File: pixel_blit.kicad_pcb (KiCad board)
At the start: 4 copper layers, 175.5 x 122 mm, 193 parts, among them CN1 PJ-3059-B, CN2 PJ-3059-B, J1 Conn_01x03_Pin, SW1 K2-1808SN-A4SW, SW2 DSWB04LHGET, SW3 K2-1808SN-A4SW, SW4 K2-1808SN-A4SW, U1 RP2350B_C42415655, U10 DB301V-3.5-3P-GN, U11 DB301V-3.5-3P-GN, U12 DB301V-3.5-3P-GN, U13 DB301V-3.5-3P-GN, U14 DB301V-3.5-3P-GN, U15 DB301V-3.5-3P-GN, U16 DB301V-3.5-3P-GN, U17 DB301V-3.5-3P-GN, U18 DB301V-3.5-3P-GN, U19 DB301V-3.5-3P-GN, U2 W25Q128JVSIQTR, U20 DB301V-3.5-3P-GN, U21 DB301V-3.5-3P-GN, U22 DB301V-3.5-3P-GN, U23 DB301V-3.5-3P-GN, U24 DB301V-3.5-3P-GN, U25 DB301V-3.5-3P-GN, U26 DB301V-3.5-3P-GN, U27 DB301V-3.5-3P-GN, U28 DB301V-3.5-3P-GN, U29 DB301V-3.5-3P-GN, U3 TPS63070RNMR, U30 DB301V-3.5-3P-GN, U31 DB301V-3.5-3P-GN, U32 DB301V-3.5-3P-GN, U33 DB301V-3.5-3P-GN, U34 DB301V-3.5-3P-GN, U35 DB301V-3.5-3P-GN, U36 DB301V-3.5-3P-GN, U37 DB301V-3.5-3P-GN, U38 DB301V-3.5-3P-GN, U39 DB301V-3.5-3P-GN, U40 DB301V-3.5-3P-GN, U41 DSLVDS1048PWR, U42 DSLVDS1047PWR, U43 DBT10-7.62-2P, U44 DBT10-7.62-2P, U45 DBT10-7.62-2P, U46 DBT10-7.62-2P, U47 2.54-1*4, U48 2.54-1*4, U49 2.54-1*4, U5 SN74LVC8T245PWR, U50 LMV358IDR, U6 SN74LVC8T245PWR, U7 SN74LVC8T245PWR, U8 SN74LVC8T245PWR, U9 DB301V-3.5-3P-GN

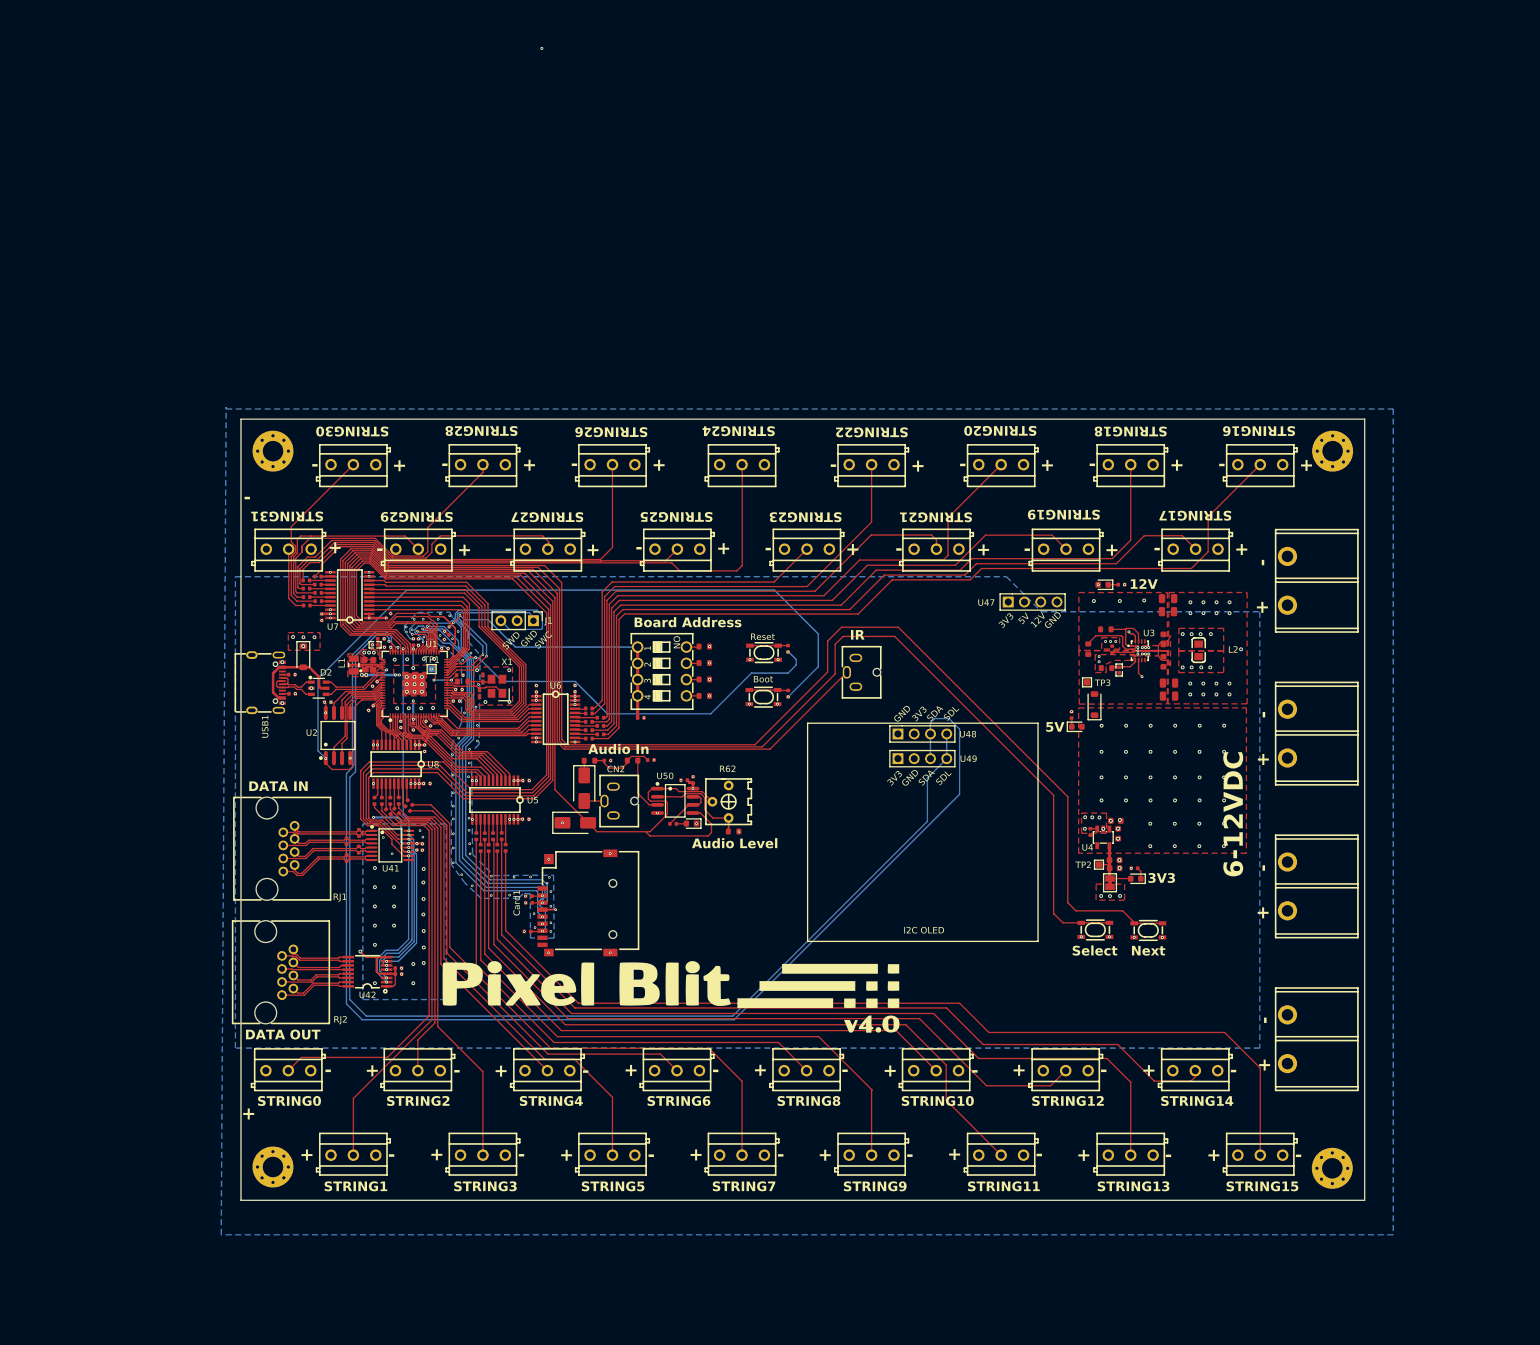
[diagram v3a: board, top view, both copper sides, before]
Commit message: Beef up power plane
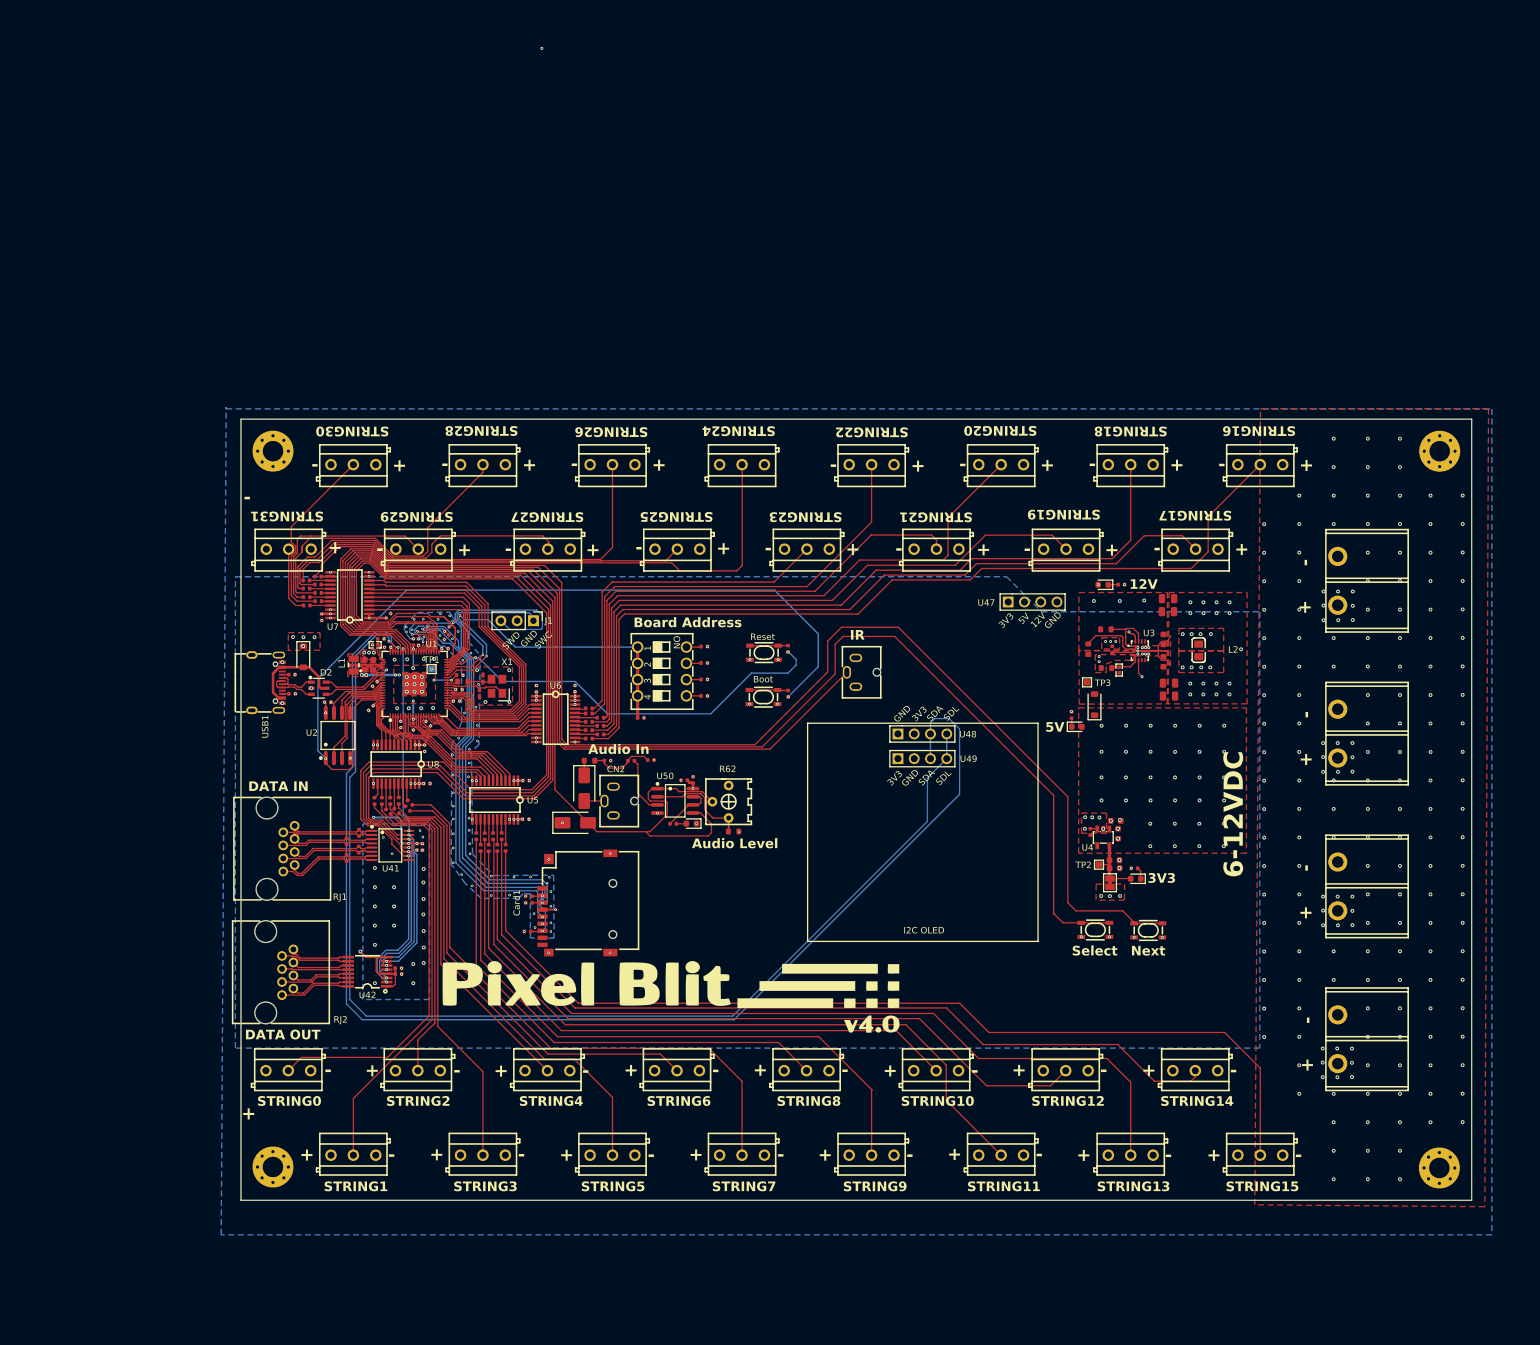
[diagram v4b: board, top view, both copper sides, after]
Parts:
- R2, R3, R4, R5, R66: footprint PCM_JLCPCB:R_0603 -> PCM_JLCPCB:R_0402
- moved H2 16.7 mm to (240.1, 36.2)
- moved H1 16.7 mm to (240.0, 148.2)
- moved U43 7.85 mm to (224.2, 56.4)
- moved U44 7.85 mm to (224.2, 80.3)
- moved U45 7.85 mm to (224.2, 104.2)
- moved U46 7.85 mm to (224.2, 128.0)
- moved R66 0.22 mm to (113.8, 84.5)
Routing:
- net +12V: vias 4 -> 192
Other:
- board size 175.5 x 122 mm -> 192.2 x 122 mm

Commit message: Library shuffle and Fabrication Toolkit micro adjustments
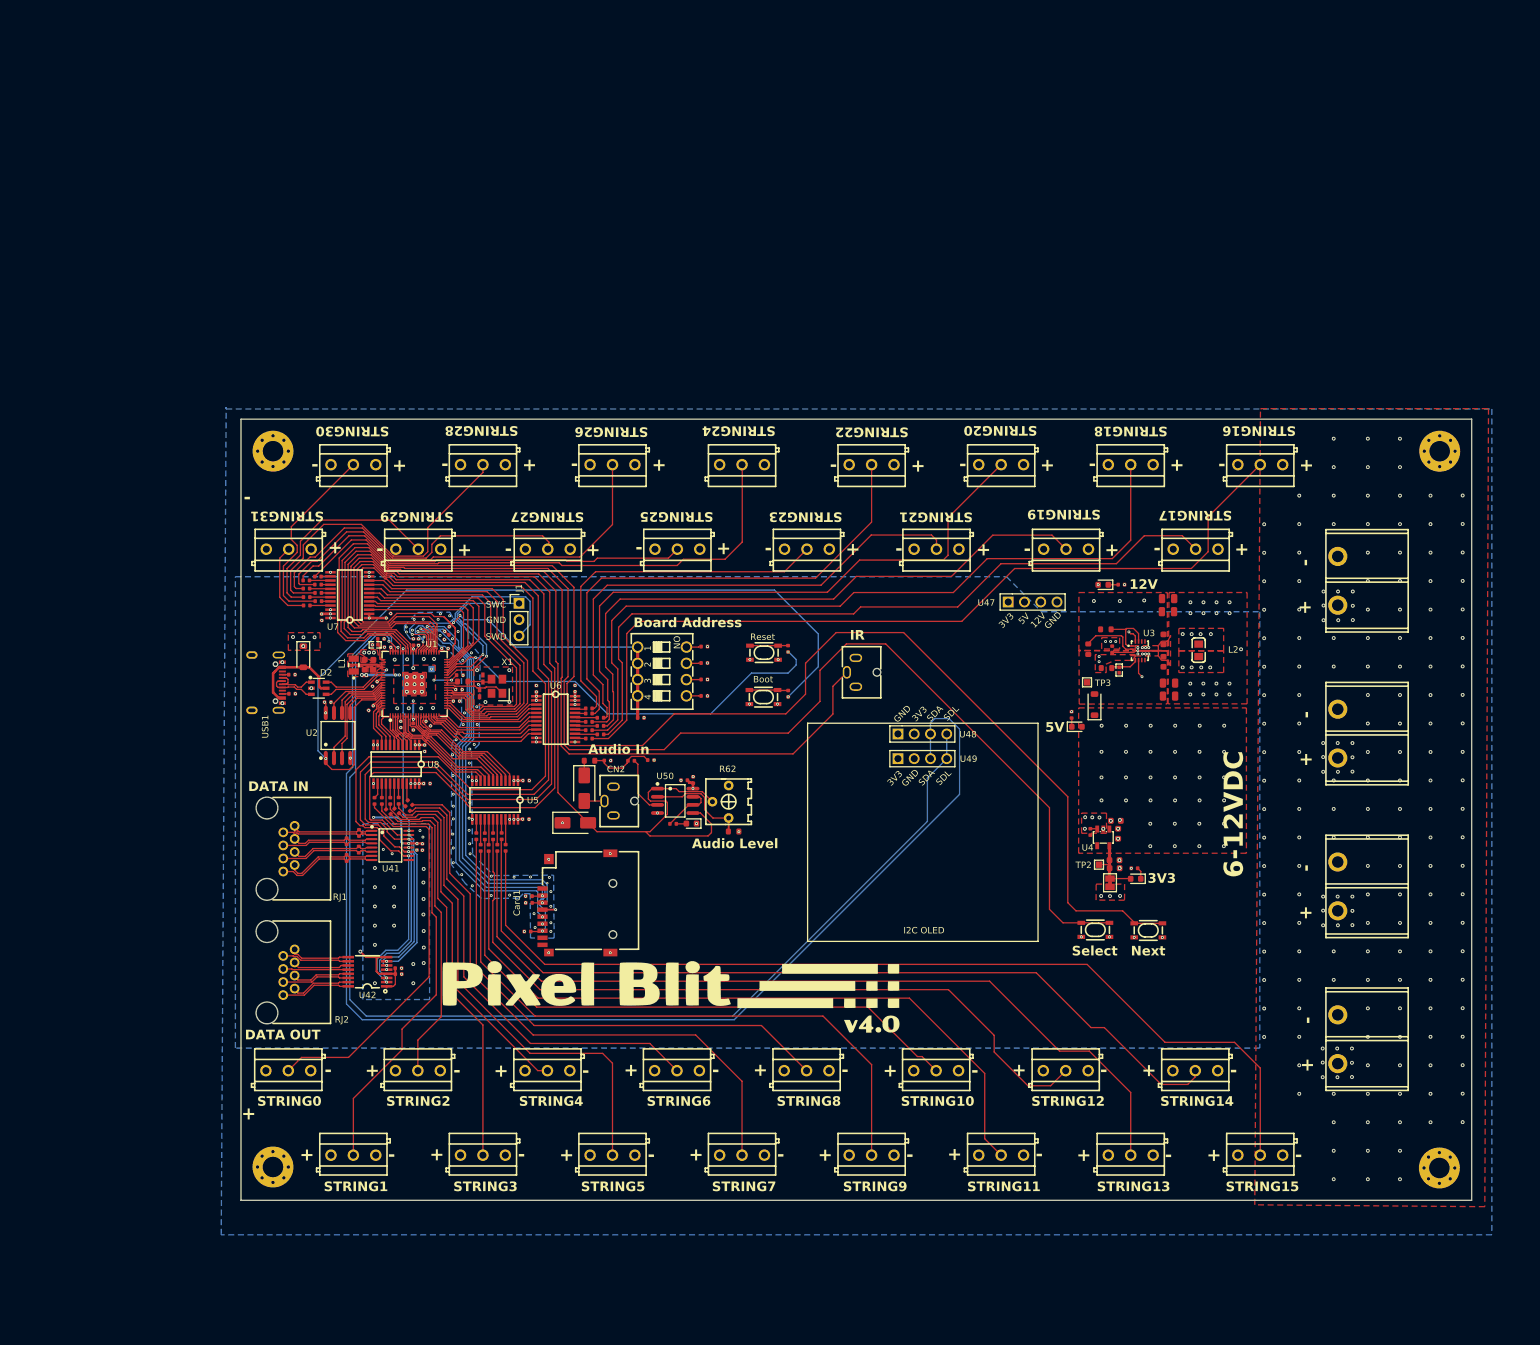
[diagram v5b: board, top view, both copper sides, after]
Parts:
- C1, C10, C11, C12, C13, C14, C2, C25, C3, C30, C31, C32, C33, C34, C35, C36, C37, C38, C39, C4, C40, C41, C42, C43, C44, C45, C5, C6, C7, C8, C9: footprint PCM_JLCPCB:C_0402 -> PixelBlit:C_0402
- C15, C16, C19, C24, C26, C27, C28, C29: footprint PCM_JLCPCB:C_0603 -> PixelBlit:C_0603
- C17, C18: footprint EasyEDA:C0402 -> PixelBlit:C0402
- C20, C21, C22, C23: footprint PCM_JLCPCB:C_0805 -> PixelBlit:C_0805
- CN1, CN2: footprint EasyEDA:AUDIO-TH_XKB_PJ-3059-B -> PixelBlit:AUDIO-TH_XKB_PJ-3059-B
- Card1: footprint EasyEDA:TF-SMD_TF-PUSH -> PixelBlit:TF-SMD_TF-PUSH
- D1, D3: footprint PCM_JLCPCB:D_SOD-123 -> PixelBlit:D_SOD-123
- D2: footprint EasyEDA:SOT-23-6_L2.9-W1.6-P0.95-LS2.8-BL -> PixelBlit:SOT-23-6_L2.9-W1.6-P0.95-LS2.8-BL
- D4, D5: footprint PCM_JLCPCB:D_SMA -> PixelBlit:D_SMA
- D6, PWR_LED1, PWR_LED2, PWR_LED3: footprint PCM_JLCPCB:D_0603 -> PixelBlit:D_0603
- G***: footprint EasyEDA:pixelblitlogo -> PixelBlit:pixelblitlogo
- H1, H2, H3, H4: footprint MountingHole:MountingHole_3.2mm_M3_Pad_Via -> PixelBlit:MountingHole_3.2mm_M3_Pad_Via
- J1: footprint Connector_PinHeader_2.54mm:PinHeader_1x03_P2.54mm_Vertical -> PixelBlit:PinHeader_1x03_P2.54mm_Vertical
- JP1: footprint Jumper:SolderJumper-2_P1.3mm_Bridged_Pad1.0x1.5mm -> PixelBlit:SolderJumper-2_P1.3mm_Bridged_Pad1.0x1.5mm
- L1: footprint EasyEDA:IND-SMD_L2.0-W1.6_AOTA-B201610S3R3-101-T -> PixelBlit:IND-SMD_L2.0-W1.6_AOTA-B201610S3R3-101-T
- L2: footprint EasyEDA:L0805 -> PixelBlit:L0805
- R1, R14, R15, R16, R17, R18, R19, R2, R20, R21, R22, R23, R24, R25, R26, R27, R28, R29, R3, R30, R31, R32, R33, R34, R35, R36, R37, R38, R39, R4, R40, R41, R42, R43, R44, R45, R46, R47, R48, R49, R5, R50, R51, R52, R53, R54, R55, R56, R57, R58, R59, R65, R66, R67, R7, R8: footprint PCM_JLCPCB:R_0402 -> PixelBlit:R_0402
- R10, R11, R13, R60, R61, R9: footprint PCM_JLCPCB:R_0603 -> PixelBlit:R_0603
- R12, R6: footprint EasyEDA:R0402 -> PixelBlit:R0402
- R62: footprint EasyEDA:RES-ADJ-TH_3362P -> PixelBlit:RES-ADJ-TH_3362P
- RJ1, RJ2: footprint EasyEDA:RJ45-TH_R-RJ45R08P-A004 -> PixelBlit:RJ45-TH_R-RJ45R08P-A004
- Reset1, SW1, SW3, SW4: footprint EasyEDA:KEY-SMD_4P-L4.2-W3.2-P2.20-LS5.1-TL -> PixelBlit:KEY-SMD_4P-L4.2-W3.2-P2.20-LS5.1-TL
- SW2: footprint EasyEDA:SW-TH_DSWB04LHGET -> PixelBlit:SW-TH_DSWB04LHGET
- TP1, TP2, TP3: footprint TestPoint:TestPoint_Pad_1.0x1.0mm -> PixelBlit:TestPoint_Pad_1.0x1.0mm
- U1: footprint EasyEDA:QFN-80_L10.0-W10.0-P0.40-TL-EP3.4 -> PixelBlit:QFN-80_L10.0-W10.0-P0.40-TL-EP3.4
- U10, U11, U12, U13, U14, U15, U16, U17, U18, U19, U20, U21, U22, U23, U24, U25, U26, U27, U28, U29, U30, U31, U32, U33, U34, U35, U36, U37, U38, U39, U40, U9: footprint EasyEDA:CONN-TH_DB301V-3.5-3P-GN -> PixelBlit:CONN-TH_DB301V-3.5-3P-GN
- U2: footprint EasyEDA:SOIC-8_L5.3-W5.3-P1.27-LS8.0-BL -> PixelBlit:SOIC-8_L5.3-W5.3-P1.27-LS8.0-BL
- U3: footprint EasyEDA:VQFN-HR-15_L3.0-W2.5-P0.50-BL_TPS63070RNMR -> PixelBlit:VQFN-HR-15_L3.0-W2.5-P0.50-BL_TPS63070RNMR
- U4: footprint EasyEDA:SOT-23-5_L3.0-W1.7-P0.95-LS2.8-BR -> PixelBlit:SOT-23-5_L3.0-W1.7-P0.95-LS2.8-BR
- U41: footprint EasyEDA:TSSOP-16_L5.0-W4.4-P0.65-LS6.4-BL -> PixelBlit:TSSOP-16_L5.0-W4.4-P0.65-LS6.4-BL
- U42: footprint EasyEDA:TSSOP-16_L5.0-W4.4-P0.65-LS6.4-TL -> PixelBlit:TSSOP-16_L5.0-W4.4-P0.65-LS6.4-TL
- U43, U44, U45, U46: footprint EasyEDA:CONN-TH_2P-P7.62_DBT10-7.62-2P -> PixelBlit:CONN-TH_2P-P7.62_DBT10-7.62-2P
- U47, U48, U49: footprint EasyEDA:HDR-TH_4P-P2.54-V-M-1 -> PixelBlit:HDR-TH_4P-P2.54-V-M-1
- U5, U6, U7, U8: footprint EasyEDA:TSSOP-24_L7.8-W4.4-P0.65-LS6.4-BL -> PixelBlit:TSSOP-24_L7.8-W4.4-P0.65-LS6.4-BL
- U50: footprint EasyEDA:SOIC-8_L4.9-W3.9-P1.27-LS6.0-BL -> PixelBlit:SOIC-8_L4.9-W3.9-P1.27-LS6.0-BL
- USB1: footprint EasyEDA:USB-C-SMD_TYPE-C-6PIN-2MD-073 -> PixelBlit:USB-C-SMD_TYPE-C-6PIN-2MD-073
- X1: footprint EasyEDA:CRYSTAL-SMD_4P-L3.2-W2.5-BL -> PixelBlit:CRYSTAL-SMD_4P-L3.2-W2.5-BL
- moved J1 3.52 mm to (96.3, 60.0), turned to 0 degrees
- moved RJ2 0.20 mm to (60.3, 117.6)
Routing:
- net IR_IN: track 132.1 -> 137.5 mm
- net Net-(R28-Pad2): track 73.9 -> 79.1 mm
- net Net-(R46-Pad2): track 53.8 -> 58.3 mm
- net SWDIO: track 38.6 -> 34.4 mm
- net NEXT_BTN: track 217.6 -> 221.3 mm
- net Net-(R45-Pad2): track 74.8 -> 78.4 mm
- net Net-(R19-Pad2): track 65.1 -> 61.6 mm
- net Net-(R44-Pad2): track 76.2 -> 79.3 mm
- net Net-(R52-Pad2): track 30.4 -> 33.4 mm
- net Net-(R34-Pad2): track 111.8 -> 114.6 mm
- net HS_DATA0: track 158.6 -> 161.2 mm
- net SWCLK: track 29.1 -> 26.6 mm
- net Net-(R32-Pad2): track 96.8 -> 99.1 mm
- net Net-(R47-Pad2): track 86.9 -> 84.6 mm
- net Net-(R50-Pad2): track 49.9 -> 52.0 mm
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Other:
- board text removed: "CN1"
- board text removed: "CN2"
